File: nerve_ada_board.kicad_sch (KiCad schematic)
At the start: 48 parts, among them J1 TC2050-IDC, J2 USB-C Power Only 6P, J3 CAN1, J4 Camera, J5 CAN2, SW1 SPST, SW2 SPDT, SW3 SPST, SW4 SPST, U1 LD1117S33TR_SOT223, U2 SAM-M10Q, U3 STM32F446RET, U5 XBP9B-DMWT-002, Y1 8M, Y2 32.768K

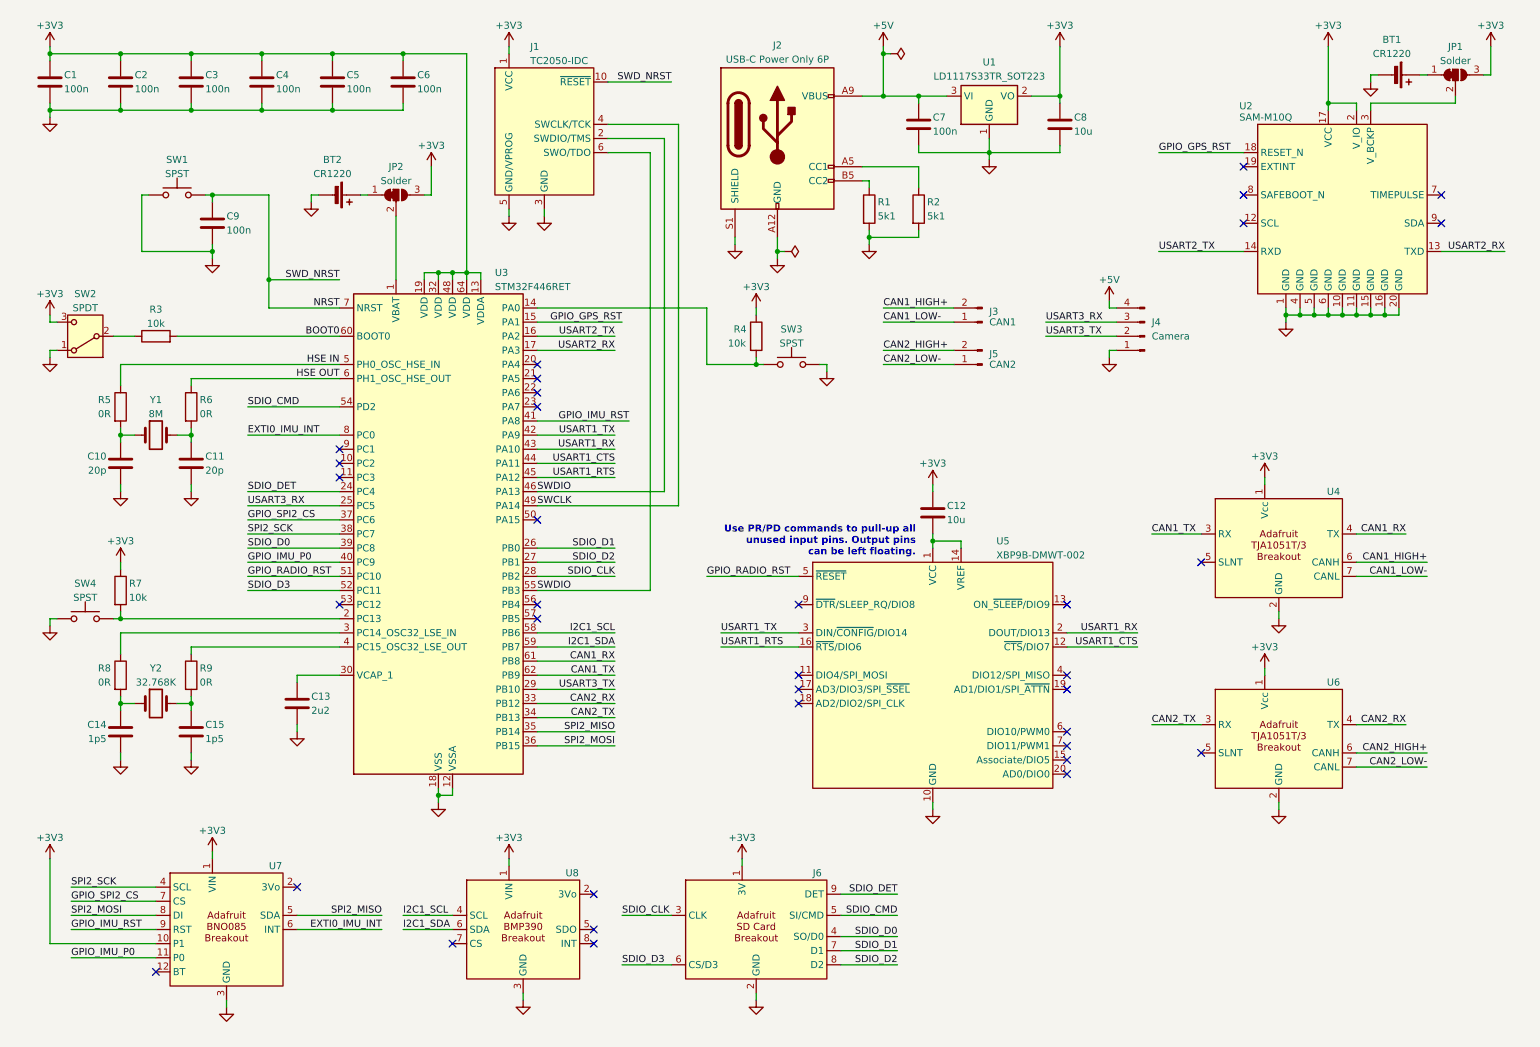
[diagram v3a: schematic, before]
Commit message: Clean up schematic
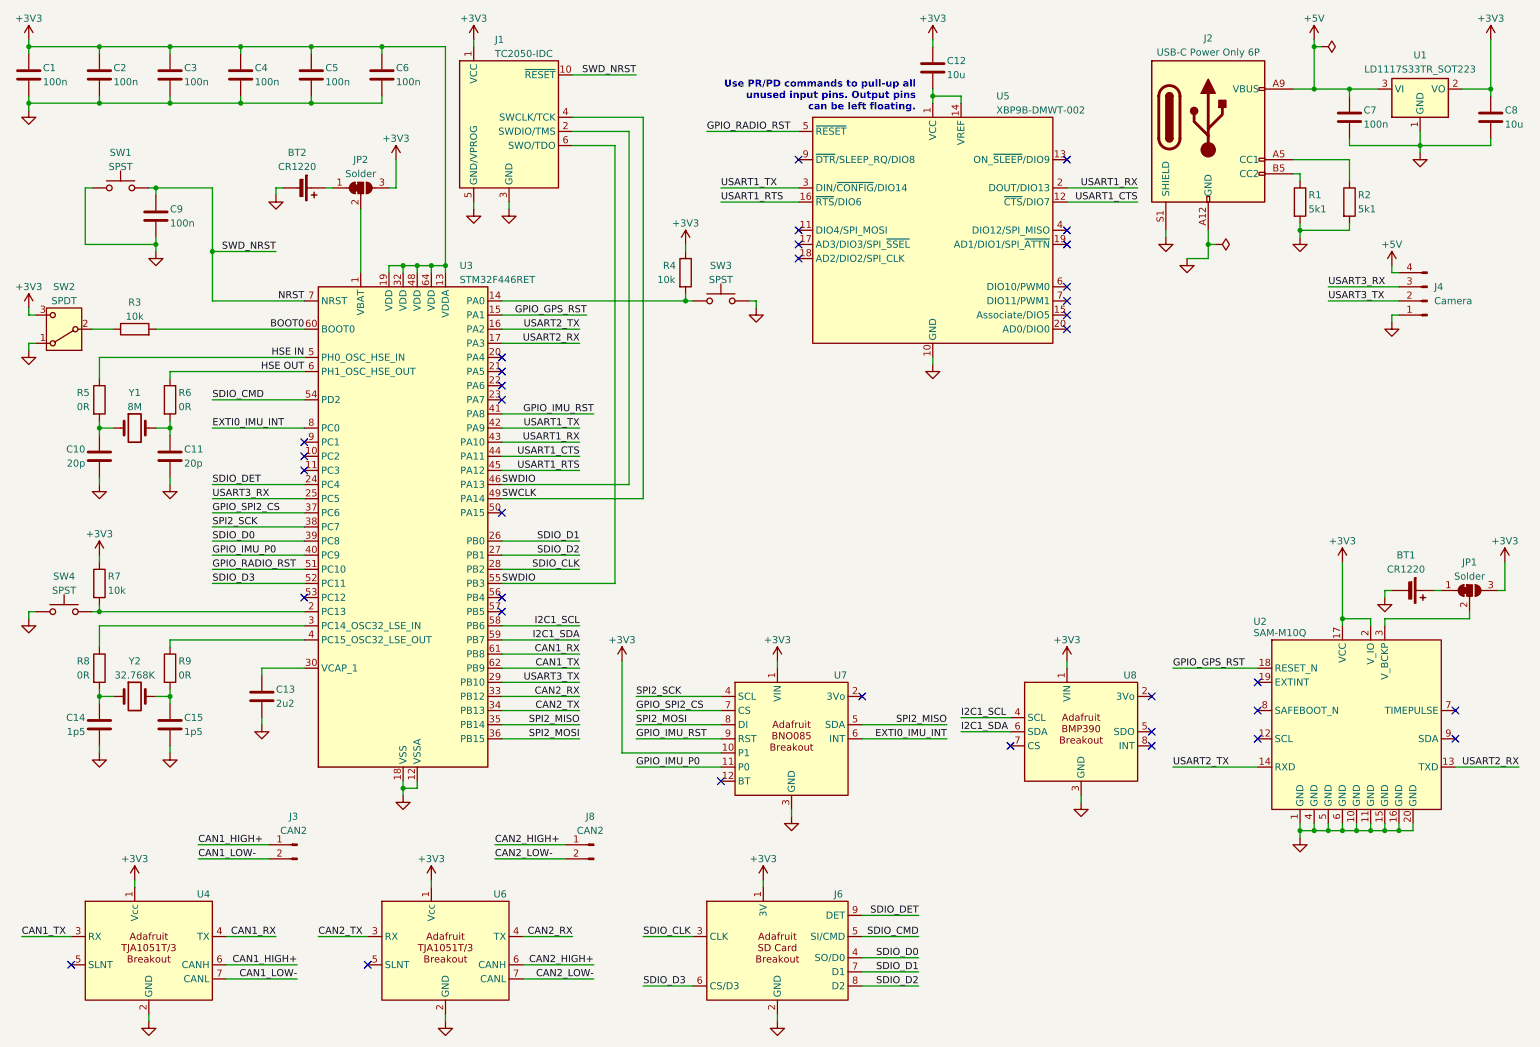
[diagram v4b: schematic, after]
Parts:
- removed J5: CAN2, symbol Connector:Conn_01x02_Pin
- added J8: CAN2, symbol Connector:Conn_01x02_Pin
- J3: value CAN1 -> CAN2
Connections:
- net CAN1_HIGH+: now also J3.1 (Pin_1); no longer J3.2 (Pin_2)
- net CAN1_LOW-: now also J3.2 (Pin_2); no longer J3.1 (Pin_1)
- net CAN2_HIGH+: now also J8.1 (Pin_1)
- net CAN2_LOW-: now also J8.2 (Pin_2)
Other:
- moved on the sheet: BT1, BT2, C1, C10, C11, C12, C13, C14, C15, C2, C3, C4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

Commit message: Add WS2812B RGB LEDs
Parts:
- added D1, D2, D3, D4, D5: WS2812B, LED_SMD:LED_WS2812B_PLCC4_5.0x5.0mm_P3.2mm, symbol LED:WS2812B
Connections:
- net +3V3: now also D1.1 (VDD), D2.1 (VDD), D3.1 (VDD), D4.1 (VDD), D5.1 (VDD)
- net GND: now also D1.3 (VSS), D2.3 (VSS), D3.3 (VSS), D4.3 (VSS), D5.3 (VSS)
- net GPIO_IMU_RST: now also U3.50 (PA15); no longer U3.41 (PA8)
- new net: D3.2 (DOUT), D4.4 (DIN)
- new net: D2.2 (DOUT), D3.4 (DIN)
- new net: D4.2 (DOUT), D5.4 (DIN)
- new net: D1.2 (DOUT), D2.4 (DIN)
- new net TIM1_CH1_PWM: D1.4 (DIN), U3.41 (PA8)

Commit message: Remove battery jumpers and fix WS2812B power
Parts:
- removed JP1, JP2: Solder, symbol Jumper:SolderJumper_3_Bridged12
- renumbered BT2 to BT1, BT1 to BT2, C12 to C1, C9 to C10, C10 to C11, C11 to C12, C1 to C2, C2 to C3, C3 to C4, C4 to C5, C5 to C6, C6 to C7, C7 to C8, C8 to C9, J4 to J3, J3 to J4, J8 to J5, R4 to R3, R3 to R4, SW3 to SW2, SW2 to SW3, U5 to U2, U2 to U4, U8 to U5, U7 to U6, U4 to U7, U6 to U8
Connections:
- net +3V3: no longer D1.1 (VDD), D2.1 (VDD), D3.1 (VDD), D4.1 (VDD), D5.1 (VDD)
- net +5V: now also D1.1 (VDD), D2.1 (VDD), D3.1 (VDD), D4.1 (VDD), D5.1 (VDD)
- net at BT1.1 (+): now also U3.1 (VBAT)
- net at U4.3 (V_BCKP): now also BT2.1 (+)
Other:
- moved on the sheet: BT1, BT2

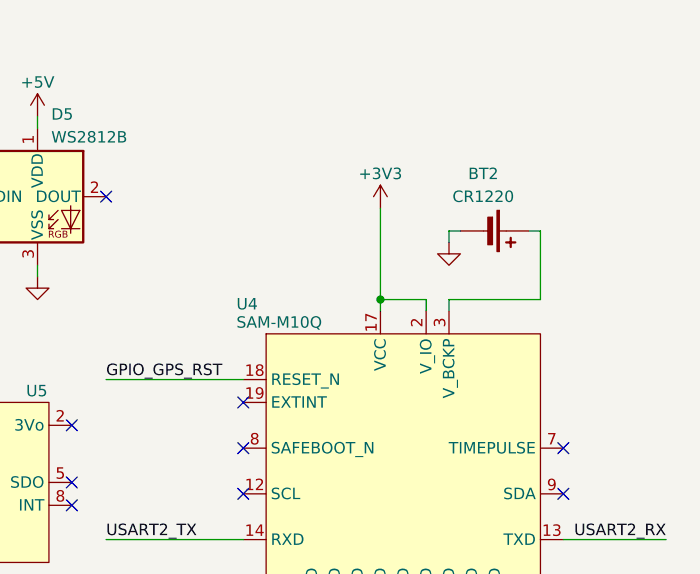
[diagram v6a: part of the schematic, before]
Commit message: Update and organize symbols on schematic
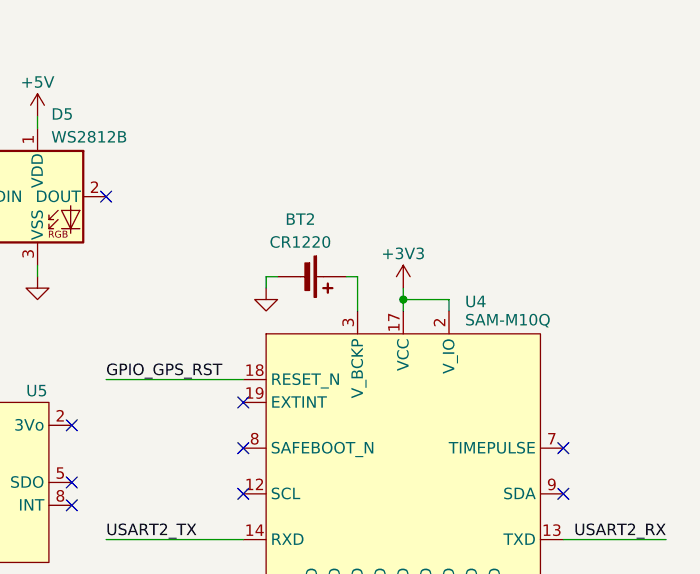
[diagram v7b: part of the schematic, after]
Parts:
- U4: footprint (none) -> ublox:ublox_sam
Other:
- moved on the sheet: BT2
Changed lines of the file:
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@@
 	)
 	(junction
-		(at 251.46 121.92)
+		(at 254 121.92)
 		(diameter 0)
 		(color 0 0 0 0)
@@
 	(wire
 		(pts
-			(xy 256.54 121.92) (xy 251.46 121.92)
+			(xy 259.08 121.92) (xy 254 121.92)
 		)
 		(stroke
@@
 	(wire
 		(pts
-			(xy 269.24 114.3) (xy 269.24 121.92)
+			(xy 82.55 152.4) (xy 82.55 153.67)
 		)
 		(stroke
@@
 	(wire
 		(pts
-			(xy 82.55 152.4) (xy 82.55 153.67)
+			(xy 120.65 36.83) (xy 120.65 115.57)
 		)
 		(stroke
@@
 	(wire
 		(pts
-			(xy 120.65 36.83) (xy 120.65 115.57)
+			(xy 40.64 87.63) (xy 38.1 87.63)
 		)
 		(stroke
@@
 	(wire
 		(pts
-			(xy 40.64 87.63) (xy 38.1 87.63)
+			(xy 133.35 64.77) (xy 134.62 64.77)
 		)
 		(stroke
@@
 	(wire
 		(pts
-			(xy 133.35 64.77) (xy 134.62 64.77)
+			(xy 48.26 82.55) (xy 64.77 82.55)
 		)
 		(stroke
@@
 	(wire
 		(pts
-			(xy 48.26 82.55) (xy 64.77 82.55)
+			(xy 227.33 52.07) (xy 227.33 54.61)
 		)
 		(stroke
@@
 	(wire
 		(pts
-			(xy 227.33 52.07) (xy 227.33 54.61)
+			(xy 15.24 67.31) (xy 16.51 67.31)
 		)
 		(stroke
@@
 	(wire
 		(pts
-			(xy 15.24 67.31) (xy 16.51 67.31)
+			(xy 254 120.65) (xy 254 121.92)
 		)
 		(stroke
@@
 	(wire
 		(pts
-			(xy 251.46 121.92) (xy 251.46 123.19)
+			(xy 254 121.92) (xy 254 123.19)
 		)
 		(stroke
@@
 	(wire
 		(pts
+			(xy 248.92 119.38) (xy 248.92 123.19)
+		)
+		(stroke
+			(width 0)
+			(type default)
+		)
+	)
+	(wire
+		(pts
 			(xy 252.73 36.83) (xy 265.43 36.83)
 		)
@@
 	(wire
 		(pts
-			(xy 259.08 121.92) (xy 259.08 123.19)
-		)
-		(stroke
-			(width 0)
-			(type default)
-		)
-	)
-	(wire
-		(pts
 			(xy 100.33 69.85) (xy 114.3 69.85)
 		)
@@
 	(wire
 		(pts
-			(xy 256.54 123.19) (xy 256.54 121.92)
+			(xy 259.08 123.19) (xy 259.08 121.92)
 		)
 		(stroke
@@
 	(wire
 		(pts
-			(xy 259.08 114.3) (xy 259.08 115.57)
+			(xy 238.76 119.38) (xy 238.76 120.65)
 		)
 		(stroke
@@
 	(wire
 		(pts
-			(xy 269.24 121.92) (xy 259.08 121.92)
-		)
-		(stroke
-			(width 0)
-			(type default)
-		)
-	)
-	(wire
-		(pts
 			(xy 27.94 87.63) (xy 27.94 88.9)
 		)
@@
 	(wire
 		(pts
-			(xy 260.35 114.3) (xy 259.08 114.3)
+			(xy 240.03 119.38) (xy 238.76 119.38)
 		)
 		(stroke
@@
 	(wire
 		(pts
-			(xy 251.46 111.76) (xy 251.46 121.92)
-		)
-		(stroke
-			(width 0)
-			(type default)
-		)
-	)
-	(wire
-		(pts
 			(xy 100.33 72.39) (xy 114.3 72.39)
 		)
@@
 	(wire
 		(pts
-			(xy 267.97 114.3) (xy 269.24 114.3)
+			(xy 247.65 119.38) (xy 248.92 119.38)
 		)
 		(stroke
@@
 		(dnp no)
 		(fields_autoplaced yes)
-		(property "Reference" "#PWR032"
+		(property "Reference" "#PWR030"
 			(at 147.32 125.73 0)
 			(effects
@@
 			(project "nerve_ada_board"
 				(path "/c0277862-b3f2-4e0e-986f-34702f0543f0"
-					(reference "#PWR032")
+					(reference "#PWR030")
 					(unit 1)
 				)
@@
 	(symbol
 		(lib_id "power:+3V3")
-		(at 251.46 111.76 0)
+		(at 254 120.65 0)
 		(unit 1)
 		(exclude_from_sim no)
@@
 		(on_board yes)
 		(dnp no)
-		(property "Reference" "#PWR030"
-			(at 251.46 115.57 0)
+		(property "Reference" "#PWR036"
+			(at 254 124.46 0)
 			(effects
 				(font
@@
 		)
 		(property "Value" "+3V3"
-			(at 251.46 107.95 0)
+			(at 254 116.84 0)
 			(effects
 				(font
@@
 		)
 		(property "Footprint" ""
-			(at 251.46 111.76 0)
+			(at 254 120.65 0)
 			(effects
 				(font
@@
 		)
 		(property "Datasheet" ""
-			(at 251.46 111.76 0)
+			(at 254 120.65 0)
 			(effects
 				(font
@@
 		)
 		(property "Description" "Power symbol creates a global label with name \"+3V3\""
-			(at 251.46 111.76 0)
+			(at 254 120.65 0)
 			(effects
 				(font
@@
 			(project "nerve_ada_board"
 				(path "/c0277862-b3f2-4e0e-986f-34702f0543f0"
-					(reference "#PWR030")
+					(reference "#PWR036")
 					(unit 1)
 				)
@@
 		(dnp no)
 		(fields_autoplaced yes)
-		(property "Reference" "#PWR035"
+		(property "Reference" "#PWR033"
 			(at 196.85 125.73 0)
 			(effects
@@
 			(project "nerve_ada_board"
 				(path "/c0277862-b3f2-4e0e-986f-34702f0543f0"
-					(reference "#PWR035")
+					(reference "#PWR033")
 					(unit 1)
 				)
@@
 		(dnp no)
 		(property "Reference" "U4"
-			(at 235.458 122.428 0)
+			(at 260.858 122.174 0)
 			(effects
 				(font
@@
 		)
 		(property "Value" "SAM-M10Q"
-			(at 235.458 124.46 0)
+			(at 260.858 124.206 0)
 			(effects
 				(font
@@
 			)
 		)
-		(property "Footprint" ""
+		(property "Footprint" "ublox:ublox_sam"
 			(at 254 140.97 0)
 			(effects
@@
 	(symbol
 		(lib_id "Device:Battery_Cell")
-		(at 262.89 114.3 270)
+		(at 242.57 119.38 270)
 		(unit 1)
 		(exclude_from_sim no)
@@
 		(dnp no)
 		(property "Reference" "BT2"
-			(at 262.89 107.95 90)
+			(at 242.57 113.03 90)
 			(effects
 				(font
@@
 		)
 		(property "Value" "CR1220"
-			(at 262.89 110.49 90)
+			(at 242.57 115.57 90)
 			(effects
 				(font
@@
 		)
 		(property "Footprint" ""
-			(at 264.414 114.3 90)
+			(at 244.094 119.38 90)
 			(effects
 				(font
@@
 		)
 		(property "Datasheet" "~"
-			(at 264.414 114.3 90)
+			(at 244.094 119.38 90)
 			(effects
 				(font
@@
 		)
 		(property "Description" "Single-cell battery"
-			(at 262.89 114.3 0)
+			(at 242.57 119.38 0)
 			(effects
 				(font
@@
 		(dnp no)
 		(fields_autoplaced yes)
-		(property "Reference" "#PWR033"
+		(property "Reference" "#PWR031"
 			(at 163.83 125.73 0)
 			(effects
@@
 			(project "nerve_ada_board"
 				(path "/c0277862-b3f2-4e0e-986f-34702f0543f0"
-					(reference "#PWR033")
+					(reference "#PWR031")
 					(unit 1)
 				)
@@
 	(symbol
 		(lib_id "power:GND")
-		(at 259.08 115.57 0)
+		(at 238.76 120.65 0)
 		(unit 1)
 		(exclude_from_sim no)
@@
 		(dnp no)
 		(fields_autoplaced yes)
-		(property "Reference" "#PWR031"
-			(at 259.08 121.92 0)
+		(property "Reference" "#PWR035"
+			(at 238.76 127 0)
 			(effects
 				(font
@@
 		)
 		(property "Value" "GND"
-			(at 259.08 120.65 0)
+			(at 238.76 125.73 0)
 			(effects
 				(font
@@
 		)
 		(property "Footprint" ""
-			(at 259.08 115.57 0)
+			(at 238.76 120.65 0)
 			(effects
 				(font
@@
 		)
 		(property "Datasheet" ""
-			(at 259.08 115.57 0)
+			(at 238.76 120.65 0)
 			(effects
 				(font
@@
 		)
 		(property "Description" "Power symbol creates a global label with name \"GND\" , ground"
-			(at 259.08 115.57 0)
+			(at 238.76 120.65 0)
 			(effects
 				(font
@@
 			(project "nerve_ada_board"
 				(path "/c0277862-b3f2-4e0e-986f-34702f0543f0"
-					(reference "#PWR031")
+					(reference "#PWR035")
 					(unit 1)
 				)
@@
 		(dnp no)
 		(fields_autoplaced yes)
-		(property "Reference" "#PWR036"
+		(property "Reference" "#PWR034"
 			(at 213.36 125.73 0)
 			(effects
@@
 			(project "nerve_ada_board"
 				(path "/c0277862-b3f2-4e0e-986f-34702f0543f0"
-					(reference "#PWR036")
+					(reference "#PWR034")
 					(unit 1)
 				)
@@
 		(dnp no)
 		(fields_autoplaced yes)
-		(property "Reference" "#PWR034"
+		(property "Reference" "#PWR032"
 			(at 180.34 125.73 0)
 			(effects
@@
 			(project "nerve_ada_board"
 				(path "/c0277862-b3f2-4e0e-986f-34702f0543f0"
-					(reference "#PWR034")
+					(reference "#PWR032")
 					(unit 1)
 				)
